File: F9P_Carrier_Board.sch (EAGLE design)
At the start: 79 parts, among them J4 U.FL, J5 QWIIC_RIGHT_ANGLE, J6 MICROMOD-2222-C, J8 JTAG, U1 U-BLOX_ZED-F9P, U5 AP7361C-33

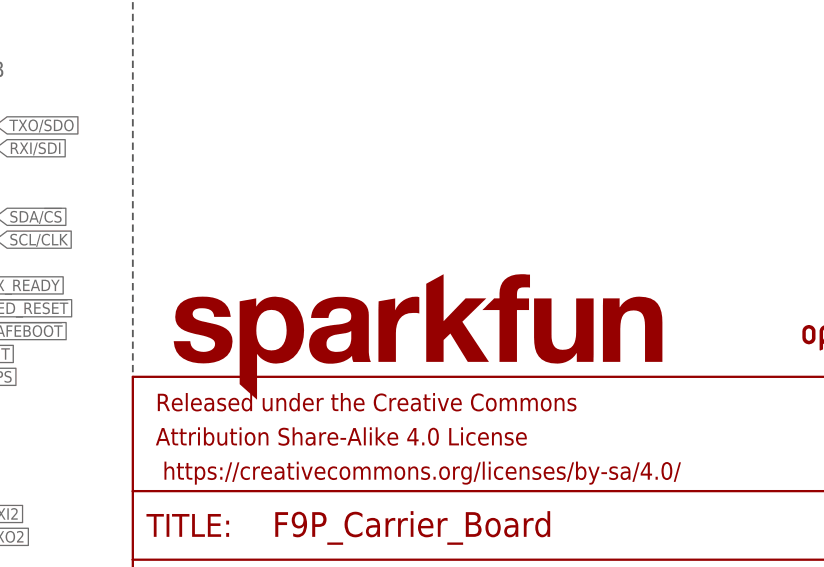
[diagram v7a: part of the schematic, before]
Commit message: Adds silk and measures
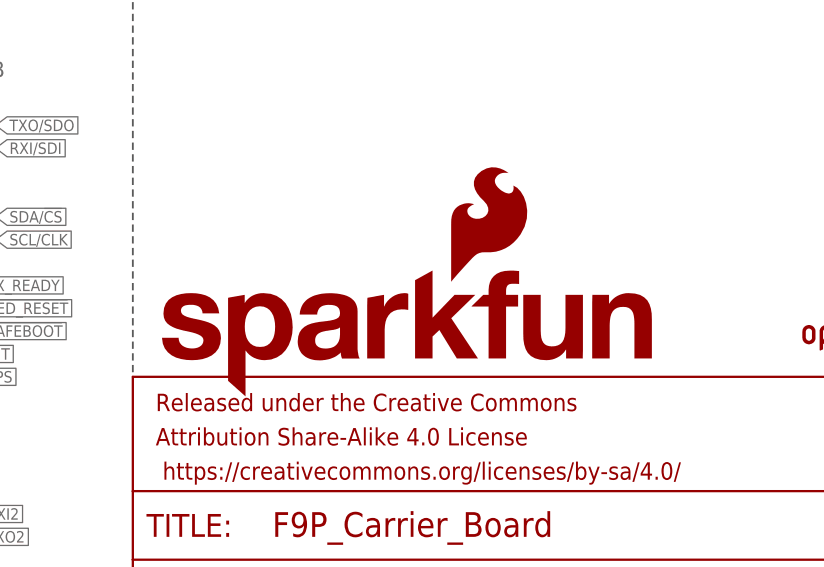
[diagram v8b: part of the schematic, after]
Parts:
- LOGO1: value SFE_LOGO_NAME.1_INCH -> SFE_LOGO_NAME_FLAME.3_INCH; device SparkFun-Aesthetics:SFE_LOGO_NAME.1_INCH -> SparkFun-Aesthetics:SFE_LOGO_NAME_FLAME.3_INCH
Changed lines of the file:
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@@
 <part name="C3" library="SparkFun-Capacitors" deviceset="0.1UF" device="-0603-25V-5%" value="0.1uF"/>
 <part name="C4" library="SparkFun-Capacitors" deviceset="0.1UF" device="-0603-25V-5%" value="0.1uF"/>
-<part name="LOGO1" library="SparkFun-Aesthetics" deviceset="SFE_LOGO_NAME" device=".1_INCH"/>
+<part name="LOGO1" library="SparkFun-Aesthetics" deviceset="SFE_LOGO_NAME_FLAME" device=".3_INCH" value="SFE_LOGO_NAME_FLAME.3_INCH"/>
 <part name="FD2" library="SparkFun-Aesthetics" deviceset="FIDUCIAL" device="UFIDUCIAL"/>
 <part name="FD4" library="SparkFun-Aesthetics" deviceset="FIDUCIAL" device="UFIDUCIAL"/>
